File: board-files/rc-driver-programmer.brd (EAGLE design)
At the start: 27 x 20.7 mm, 14 parts, among them IC1 TINY22S

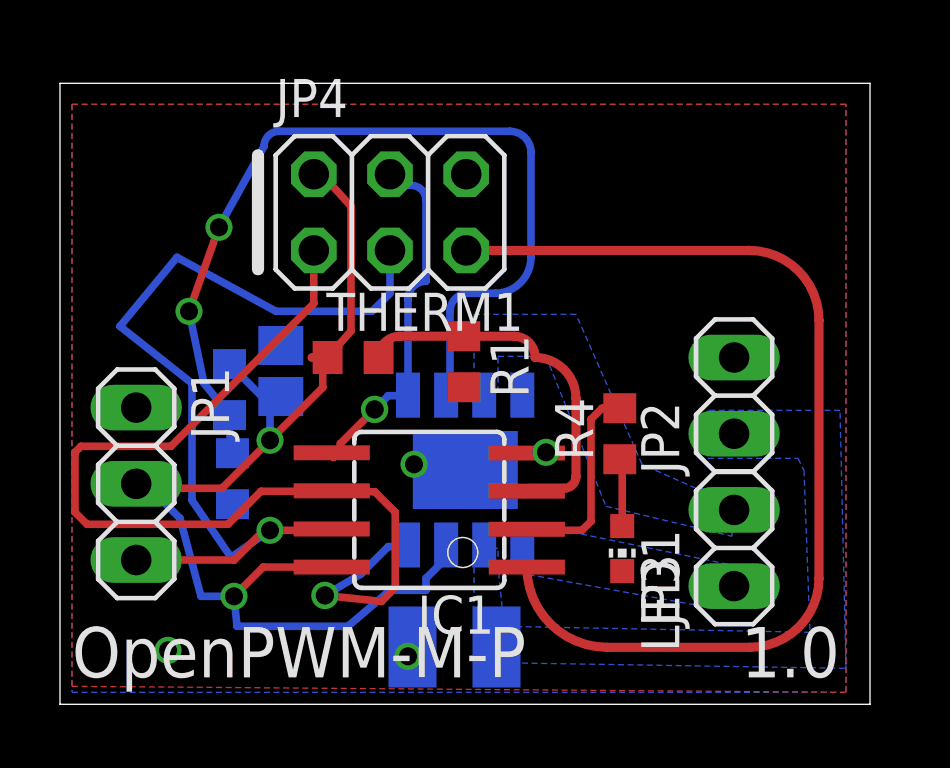
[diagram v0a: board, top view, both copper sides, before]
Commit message: Adding RC net to VREF. Creating gerbers for plain board.
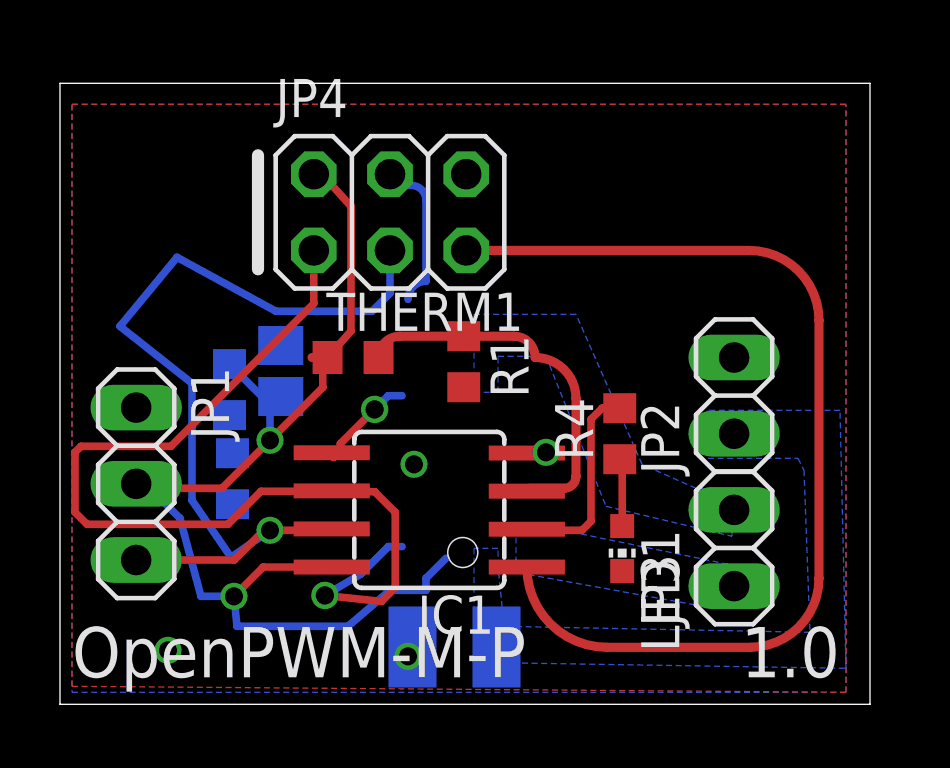
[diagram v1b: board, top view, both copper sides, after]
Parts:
- removed U$1: ZXBM5210-MOTOR-DRIVER, mgregg:SO-8EP
- R2: value (none) -> 27k
- R3: value (none) -> 10k
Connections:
- removed net N$1: R2.2, R3.1, U$1.P$6
- new net N$4: R2.2, R3.1
- net FWD: no longer U$1.P$4
- net GND: no longer U$1.P$8, U$1.PAD
- net MOTOR1-1: no longer U$1.P$1
- net MOTOR1-2: no longer U$1.P$7
- net REV: no longer U$1.P$5
- net VCC: no longer U$1.P$3
- net VM: no longer U$1.P$2
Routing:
- net N$1: track 30.6 -> 0.00 mm, vias 2 -> 0
- net REV: track 11.9 -> 8.55 mm
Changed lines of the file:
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@@
 <element name="JP1" library="pinhead" package="1X03" value="" x="2.54" y="7.35" rot="R270"/>
 <element name="JP3" library="pinhead" package="1X02" value="" x="22.47" y="5.21" rot="R90"/>
-<element name="U$1" library="mgregg" package="SO-8EP" value="ZXBM5210-MOTOR-DRIVER" x="13.37" y="7.85" rot="MR0"/>
 <element name="IC1" library="mgregg" package="SOIC8" value="TINY22S" x="12.31" y="6.48" rot="R90">
 <attribute name="OC_NEWARK" value="unknown" x="12.31" y="6.48" size="1.778" layer="27" rot="R90" display="off"/>
@@
 <element name="THERM1" library="resistor" package="R0603" value="4.7k" x="9.77" y="11.56"/>
 <element name="R1" library="resistor" package="R0603" value="20k" x="13.46" y="11.42" rot="R270"/>
-<element name="R2" library="resistor" package="R0603" value="" x="5.65" y="10.49" rot="MR270"/>
-<element name="R3" library="resistor" package="R0603" value="" x="5.75" y="7.52" rot="MR270"/>
+<element name="R2" library="resistor" package="R0603" value="27k" x="5.65" y="10.49" rot="MR270"/>
+<element name="R3" library="resistor" package="R0603" value="10k" x="5.75" y="7.52" rot="MR270"/>
 <element name="R4" library="resistor" package="R0603" value="" x="18.66" y="9.02" rot="R90"/>
 <element name="LED1" library="led" package="CHIP-LED0603" value="" x="18.74" y="5.19" rot="R180"/>
@@
 <contactref element="JP1" pad="1"/>
 <contactref element="IC1" pad="4"/>
-<contactref element="U$1" pad="P$8"/>
-<contactref element="U$1" pad="PAD"/>
 <contactref element="R1" pad="2"/>
 <contactref element="R3" pad="2"/>
@@
 <signal name="VM">
 <contactref element="C1" pad="2"/>
-<contactref element="U$1" pad="P$2"/>
 <contactref element="JP2" pad="1"/>
 <polygon width="0.254" layer="16" thermals="no">
@@
 <contactref element="JP1" pad="2"/>
 <contactref element="IC1" pad="8"/>
-<contactref element="U$1" pad="P$3"/>
 <contactref element="THERM1" pad="1"/>
 <contactref element="R2" pad="1"/>
 <wire x1="8.76" y1="11.4" x2="8.92" y2="11.56" width="0.4064" layer="1"/>
-<wire x1="12.87" y1="5.31" x2="12.87" y2="4.87" width="0.254" layer="16"/>
 <wire x1="12.87" y1="4.87" x2="12.2" y2="4.2" width="0.254" layer="16"/>
 <wire x1="12.2" y1="4.2" x2="12.2" y2="3.8" width="0.254" layer="16"/>
@@
 <signal name="MOTOR1-2">
 <contactref element="JP3" pad="2"/>
-<contactref element="U$1" pad="P$7"/>
 <polygon width="0.254" layer="16" thermals="no">
 <vertex x="14.6" y="10.4"/>
@@
 <signal name="MOTOR1-1">
 <contactref element="JP3" pad="1"/>
-<contactref element="U$1" pad="P$1"/>
 <polygon width="0.254" layer="16" thermals="no">
 <vertex x="21.8" y="3.2"/>
@@
 </signal>
 <signal name="REV">
-<contactref element="U$1" pad="P$5"/>
 <contactref element="IC1" pad="5"/>
 <wire x1="10.9448" y1="10.287" x2="11.402" y2="10.287" width="0.254" layer="16"/>
@@
 <wire x1="9.3446" y1="8.4582" x2="9.3446" y2="8.6868" width="0.254" layer="1"/>
 <wire x1="9.116" y1="8.2296" x2="9.3446" y2="8.4582" width="0.254" layer="1"/>
-<wire x1="11.402" y1="10.287" x2="11.6" y2="10.305" width="0.254" layer="16"/>
 <wire x1="9.116" y1="8.2296" x2="9.0588" y2="8.385" width="0.254" layer="1"/>
 <via x="10.4876" y="9.8298" extent="1-16" drill="0.6096"/>
@@
 <wire x1="12.2" y1="16.8" x2="12.2" y2="14.1" width="0.254" layer="16"/>
 <wire x1="12.2" y1="14.1" x2="11.6" y2="13.5" width="0.254" layer="16" curve="90"/>
-<wire x1="11.6" y1="13.5" x2="11.6" y2="10.305" width="0.254" layer="16"/>
+<wire x1="11.402" y1="10.287" x2="11.6" y2="13.5" width="0" layer="19" extent="16-16"/>
 </signal>
 <signal name="FWD">
-<contactref element="U$1" pad="P$4"/>
 <contactref element="IC1" pad="6"/>
 <wire x1="10.9448" y1="5.2578" x2="11.402" y2="5.2578" width="0.254" layer="16"/>
@@
 <wire x1="9.116" y1="7.0866" x2="9.6" y2="7.0866" width="0.254" layer="1"/>
 <wire x1="9.6" y1="7.0866" x2="10.4876" y2="7.0866" width="0.254" layer="1"/>
-<wire x1="11.402" y1="5.2578" x2="11.6" y2="5.31" width="0.254" layer="16"/>
 <wire x1="9.116" y1="7.0866" x2="9.0588" y2="7.115" width="0.254" layer="1"/>
 <via x="8.8304" y="3.629" extent="1-16" drill="0.6096"/>
@@
 <wire x1="11.33" y1="12.27" x2="10.62" y2="11.56" width="0.3048" layer="1" curve="90"/>
 </signal>
-<signal name="N$1">
-<contactref element="U$1" pad="P$6"/>
-<contactref element="R3" pad="1"/>
-<contactref element="R2" pad="2"/>
-<wire x1="12.8" y1="10.375" x2="12.87" y2="10.305" width="0.3048" layer="16"/>
-<wire x1="5.75" y1="8.37" x2="5.55" y2="9.74" width="0.254" layer="16"/>
-<wire x1="5.55" y1="9.74" x2="5.65" y2="9.64" width="0.254" layer="16"/>
-<wire x1="12.8" y1="10.375" x2="13" y2="10.575" width="0.254" layer="16" curve="90"/>
-<wire x1="13" y1="10.575" x2="13" y2="13.1" width="0.254" layer="16"/>
-<wire x1="13" y1="13.1" x2="13.6" y2="13.7" width="0.254" layer="16" curve="-90"/>
-<wire x1="13.6" y1="13.7" x2="14.5" y2="13.7" width="0.254" layer="16"/>
-<wire x1="14.5" y1="13.7" x2="15.7" y2="14.9" width="0.254" layer="16" curve="90"/>
-<wire x1="15.7" y1="14.9" x2="15.7" y2="18.4" width="0.254" layer="16"/>
-<wire x1="15.7" y1="18.4" x2="15" y2="19.1" width="0.254" layer="16" curve="90"/>
-<wire x1="15" y1="19.1" x2="7.3" y2="19.1" width="0.254" layer="16"/>
-<wire x1="7.3" y1="19.1" x2="6.8" y2="18.6" width="0.254" layer="16" curve="90"/>
-<via x="5.3" y="15.9" extent="1-16" drill="0.6"/>
-<wire x1="5.3" y1="15.9" x2="4.3" y2="13.1" width="0.254" layer="1"/>
-<via x="4.3" y="13.1" extent="1-16" drill="0.6"/>
-<wire x1="4.3" y1="13.1" x2="4.8" y2="10.7" width="0.254" layer="16"/>
-<wire x1="4.8" y1="10.7" x2="5.65" y2="9.64" width="0.254" layer="16"/>
-<wire x1="6.8" y1="18.6" x2="5.3" y2="15.9" width="0.254" layer="16"/>
-</signal>
 <signal name="N$2">
 <contactref element="IC1" pad="2"/>
@@
 <wire x1="18.74" y1="8.09" x2="18.66" y2="8.17" width="0.254" layer="1"/>
 </signal>
+<signal name="N$4">
+<contactref element="R3" pad="1"/>
+<contactref element="R2" pad="2"/>
+<wire x1="5.65" y1="9.64" x2="5.75" y2="8.37" width="0" layer="19" extent="16-16"/>
+</signal>
 </signals>
